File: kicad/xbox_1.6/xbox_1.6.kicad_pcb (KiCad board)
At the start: 2 copper layers, 18 parts, among them U2C1 intel_495_bga2, U4B1 ddr_100_tqfp, U4C1 nvidia_xgpu_nv2a, U5F1 ddr_100_tqfp, U6D1 ddr_100_tqfp, U6E1 nvidia_mcpx

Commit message: route more
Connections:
- U2C1 pad AA1: (no net) -> /CPU_AERR
- U2C1 pad AA2: (no net) -> /CPU_RS1
- U2C1 pad AA3: (no net) -> /CPU_DBSY
- U2C1 pad AA4: (no net) -> /VSS
- U2C1 pad AB1: (no net) -> /CPU_AP0
- U2C1 pad AB2: (no net) -> /CPU_ADS
- U2C1 pad AB3: (no net) -> /VSS
- U2C1 pad AB4: (no net) -> /VSS
- U2C1 pad AB5: (no net) -> /VSS
- U2C1 pad AC1: (no net) -> /VSS
- U2C1 pad AC2: (no net) -> /VSS
- U2C1 pad AC4: (no net) -> /VSS
- U2C1 pad AC5: (no net) -> /VSS
- U2C1 pad AD1: (no net) -> /VSS
- U2C1 pad AD2: (no net) -> /VSS
- U2C1 pad AD3: (no net) -> /VSS
- U2C1 pad AD4: (no net) -> /VSS
- U2C1 pad AD5: (no net) -> /VSS
- U2C1 pad H10: (no net) -> /CPU_VCC
- U2C1 pad H11: (no net) -> /VSS
- U2C1 pad H12: (no net) -> /CPU_VCC
- U2C1 pad H13: (no net) -> /VSS
- U2C1 pad H14: (no net) -> /CPU_VCC
- U2C1 pad H15: (no net) -> /VSS
- U2C1 pad H16: (no net) -> /CPU_VCC
- U2C1 pad H7: (no net) -> /VSS
- U2C1 pad H8: (no net) -> /CPU_VCC
- U2C1 pad H9: (no net) -> /VSS
- U2C1 pad J10: (no net) -> /VSS
- U2C1 pad J11: (no net) -> /CPU_VCC
- U2C1 pad J12: (no net) -> /VSS
- U2C1 pad J13: (no net) -> /CPU_VCC
- U2C1 pad J14: (no net) -> /VSS
- U2C1 pad J15: (no net) -> /CPU_VCC
- U2C1 pad J16: (no net) -> /VSS
- U2C1 pad J6: (no net) -> /CPU_VCCT
- U2C1 pad J7: (no net) -> /CPU_VCC
- U2C1 pad J8: (no net) -> /VSS
- U2C1 pad J9: (no net) -> /CPU_VCC
- U2C1 pad K10: (no net) -> /CPU_VCC
- U2C1 pad K11: (no net) -> /VSS
- U2C1 pad K12: (no net) -> /CPU_VCC
- U2C1 pad K13: (no net) -> /VSS
- U2C1 pad K14: (no net) -> /CPU_VCC
- U2C1 pad K15: (no net) -> /VSS
- U2C1 pad K16: (no net) -> /CPU_VCC
- U2C1 pad K7: (no net) -> /VSS
- U2C1 pad K8: (no net) -> /CPU_VCC
- U2C1 pad K9: (no net) -> /VSS
- U2C1 pad L10: (no net) -> /VSS
- U2C1 pad L11: (no net) -> /CPU_VCC
- U2C1 pad L12: (no net) -> /VSS
- U2C1 pad L13: (no net) -> /CPU_VCC
- U2C1 pad L14: (no net) -> /VSS
- U2C1 pad L15: (no net) -> /CPU_VCC
- U2C1 pad L16: (no net) -> /VSS
- U2C1 pad L7: (no net) -> /CPU_VCC
- U2C1 pad L8: (no net) -> /VSS
- U2C1 pad L9: (no net) -> /CPU_VCC
- U2C1 pad M10: (no net) -> /CPU_VCC
- U2C1 pad M11: (no net) -> /VSS
- U2C1 pad M12: (no net) -> /CPU_VCC
- U2C1 pad M13: (no net) -> /VSS
- U2C1 pad M14: (no net) -> /CPU_VCC
- U2C1 pad M15: (no net) -> /VSS
- U2C1 pad M16: (no net) -> /CPU_VCC
- U2C1 pad M7: (no net) -> /VSS
- U2C1 pad M8: (no net) -> /CPU_VCC
- U2C1 pad M9: (no net) -> /VSS
- U2C1 pad N10: (no net) -> /VSS
- U2C1 pad N11: (no net) -> /CPU_VCC
- U2C1 pad N12: (no net) -> /VSS
- U2C1 pad N13: (no net) -> /CPU_VCC
- U2C1 pad N14: (no net) -> /VSS
- U2C1 pad N15: (no net) -> /CPU_VCC
- U2C1 pad N16: (no net) -> /VSS
- U2C1 pad N7: (no net) -> /CPU_VCC
- U2C1 pad N8: (no net) -> /VSS
- U2C1 pad N9: (no net) -> /CPU_VCC
- U2C1 pad P10: (no net) -> /CPU_VCC
- U2C1 pad P11: (no net) -> /VSS
- U2C1 pad P12: (no net) -> /CPU_VCC
- U2C1 pad P13: (no net) -> /VSS
- U2C1 pad P14: (no net) -> /CPU_VCC
- U2C1 pad P15: (no net) -> /VSS
- U2C1 pad P16: (no net) -> /CPU_VCC
- U2C1 pad P7: (no net) -> /VSS
- U2C1 pad P8: (no net) -> /CPU_VCC
- U2C1 pad P9: (no net) -> /VSS
- U2C1 pad R10: (no net) -> /VSS
- U2C1 pad R11: (no net) -> /CPU_VCC
- U2C1 pad R12: (no net) -> /VSS
- U2C1 pad R13: (no net) -> /CPU_VCC
- U2C1 pad R14: (no net) -> /VSS
- U2C1 pad R15: (no net) -> /CPU_VCC
- U2C1 pad R16: (no net) -> /VSS
- U2C1 pad R7: (no net) -> /CPU_VCC
- U2C1 pad R8: (no net) -> /VSS
- U2C1 pad R9: (no net) -> /CPU_VCC
- U2C1 pad T10: (no net) -> /CPU_VCC
- U2C1 pad T11: (no net) -> /VSS
- U2C1 pad T12: (no net) -> /CPU_VCC
- U2C1 pad T13: (no net) -> /VSS
- U2C1 pad T14: (no net) -> /CPU_VCC
- U2C1 pad T15: (no net) -> /VSS
- U2C1 pad T16: (no net) -> /CPU_VCC
- U2C1 pad T7: (no net) -> /VSS
- U2C1 pad T8: (no net) -> /CPU_VCC
- U2C1 pad T9: (no net) -> /VSS
- U2C1 pad U10: (no net) -> /VSS
- U2C1 pad U11: (no net) -> /CPU_VCC
- U2C1 pad U12: (no net) -> /VSS
- U2C1 pad U13: (no net) -> /CPU_VCC
- U2C1 pad U14: (no net) -> /VSS
- U2C1 pad U15: (no net) -> /CPU_VCC
- U2C1 pad U16: (no net) -> /VSS
- U2C1 pad U7: (no net) -> /CPU_VCC
- U2C1 pad U8: (no net) -> /VSS
- U2C1 pad U9: (no net) -> /CPU_VCC
- U2C1 pad V1: (no net) -> /CPU_HIT
- U2C1 pad V2: (no net) -> /CPU_REQ2
- U2C1 pad V4: (no net) -> /CPU_REQ1
- U2C1 pad V5: (no net) -> /CPU_PWRGOOD
- U2C1 pad W1: (no net) -> /CPU_RS2
- U2C1 pad W2: (no net) -> /CPU_RP
- U2C1 pad W3: (no net) -> /CPU_REQ3
- U2C1 pad W4: (no net) -> /VSS
- U2C1 pad W5: (no net) -> /CPU_REQ4
- U2C1 pad Y1: (no net) -> /CPU_RSP
- U2C1 pad Y2: (no net) -> /CPU_AP1
- U2C1 pad Y3: (no net) -> /VSS
- U2C1 pad Y4: (no net) -> /CPU_HITM
- U2C1 pad Y5: (no net) -> /CPU_TESTLO1
- U4C1 pad A25: (no net) -> /CPU_HIT
- U4C1 pad A26: (no net) -> /CPU_REQ3
- U4C1 pad A27: (no net) -> /CPU_REQ4
- U4C1 pad A28: (no net) -> /CPU_DBSY
- U4C1 pad B24: (no net) -> /CPU_REQ2
- U4C1 pad B26: (no net) -> /CPU_RS2
- U4C1 pad B27: (no net) -> /CPU_ADS
- U4C1 pad B28: (no net) -> /CPU_RS1
- U4C1 pad C25: (no net) -> /CPU_REQ1
- U4C1 pad C27: (no net) -> /CPU_HITM
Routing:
- net /VSS: track 79.5 -> 166.6 mm, vias 47 -> 83
- net /CPU_REQ3: track 0.00 -> 80.7 mm, vias 0 -> 1
- net /CPU_HITM: track 0.00 -> 80.1 mm, vias 0 -> 1
- net /CPU_RS1: track 0.00 -> 80.1 mm, vias 0 -> 1
- net /CPU_ADS: track 0.00 -> 79.3 mm, vias 0 -> 1
- net /CPU_DBSY: track 0.00 -> 79.2 mm, vias 0 -> 1
- net /CPU_REQ4: track 0.00 -> 77.7 mm, vias 0 -> 1
- net /CPU_RS2: track 0.00 -> 77.4 mm, vias 0 -> 1
- net /CPU_REQ1: track 0.00 -> 77.0 mm, vias 0 -> 1
- net /CPU_VCC: track 0.00 -> 76.9 mm, vias 0 -> 16
- net /CPU_REQ2: track 0.00 -> 75.8 mm, vias 0 -> 1
- net /CPU_HIT: track 0.00 -> 75.7 mm, vias 0 -> 1
- net /CPU_AP1: track 0.00 -> 3.79 mm, vias 0 -> 1
- net /CPU_AP0: track 0.00 -> 0.85 mm, vias 0 -> 1
- net /CPU_TESTLO1: track 0.00 -> 0.84 mm, vias 0 -> 1
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
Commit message: route more
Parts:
- added C1C1: 0603_smd, xbox_footprint:0603_smd, F.Cu at (299.4, 122.5)
- added C1D1: 0603_smd, xbox_footprint:0603_smd, F.Cu at (302.0, 124.5)
- added C1D2: 0603_smd, xbox_footprint:0603_smd, F.Cu at (301.0, 130.8)
- added C1D3: 0603_smd, xbox_footprint:0603_smd, F.Cu at (295.8, 124.3)
- added R1C1: 0603_smd, xbox_footprint:0603_smd, F.Cu at (302.1, 120.7)
- added R1C10: 0603_smd, xbox_footprint:0603_smd, F.Cu at (295.9, 111.0)
- added R1C11: 0603_smd, xbox_footprint:0603_smd, F.Cu at (295.9, 113.0)
- added R1C12: 0603_smd, xbox_footprint:0603_smd, F.Cu at (295.9, 116.8)
- added R1C13: 0603_smd, xbox_footprint:0603_smd, F.Cu at (295.9, 114.8)
- added R1C14: 0603_smd, xbox_footprint:0603_smd, F.Cu at (295.8, 102.7)
- added R1C15: 0603_smd, xbox_footprint:0603_smd, F.Cu at (295.9, 101.0)
- added R1C16: 0603_smd, xbox_footprint:0603_smd, F.Cu at (295.8, 104.5)
- added R1C17: 0603_smd, xbox_footprint:0603_smd, F.Cu at (295.8, 106.3)
- added R1C2: 0603_smd, xbox_footprint:0603_smd, F.Cu at (299.5, 109.4)
- added R1C3: 0603_smd, xbox_footprint:0603_smd, F.Cu at (299.5, 111.0)
- added R1C4: 0603_smd, xbox_footprint:0603_smd, F.Cu at (299.5, 113.0)
- added R1C5: 0603_smd, xbox_footprint:0603_smd, F.Cu at (299.5, 114.8)
- added R1C6: 0603_smd, xbox_footprint:0603_smd, F.Cu at (299.5, 116.8)
- added R1C7: 0603_smd, xbox_footprint:0603_smd, F.Cu at (299.4, 118.9)
- added R1C8: 0603_smd, xbox_footprint:0603_smd, F.Cu at (299.4, 120.7)
- added R1C9: 0603_smd, xbox_footprint:0603_smd, F.Cu at (295.9, 109.2)
- added R1D1: 0603_smd, xbox_footprint:0603_smd, F.Cu at (301.1, 134.2)
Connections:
- U2C1 pad AA10: (no net) -> /CPU_INIT
- U2C1 pad AA12: (no net) -> /CPU_BSEL0
- U2C1 pad AA13: (no net) -> /VSS
- U2C1 pad AA15: (no net) -> /CPU_THERMDA
- U2C1 pad AA16: (no net) -> /CPU_EDGECTRLP
- U2C1 pad AA17: (no net) -> /CPU_BALL_AA17
- U2C1 pad AA18: (no net) -> /CPU_PICCLK
- U2C1 pad AA20: (no net) -> /VSS
- U2C1 pad AA6: (no net) -> /CPU_VCCT
- U2C1 pad AA7: (no net) -> /CPU_VCCT
- U2C1 pad AA8: (no net) -> /CPU_VCCT
- U2C1 pad AA9: (no net) -> /CPU_VREF
- U2C1 pad AB21: (no net) -> /CPU_PICD0
- U2C1 pad AD18: (no net) -> /CPU_VREF
- U2C1 pad W18: (no net) -> /VSS
- U2C1 pad W19: (no net) -> /CPU_BPM1
- U2C1 pad W20: (no net) -> /CPU_PRDY
- U2C1 pad W21: (no net) -> /CPU_BPM0
- U2C1 pad Y10: (no net) -> /VSS
- U2C1 pad Y11: (no net) -> /VSS
- U2C1 pad Y12: (no net) -> /VSS
- U2C1 pad Y13: (no net) -> /VSS
- U2C1 pad Y14: (no net) -> /VSS
- U2C1 pad Y15: (no net) -> /VSS
- U2C1 pad Y16: (no net) -> /VSS
- U2C1 pad Y17: (no net) -> /CPU_VREF
- U2C1 pad Y18: (no net) -> /CPU_VREF
- U2C1 pad Y19: (no net) -> /VSS
- U2C1 pad Y20: (no net) -> /CPU_PICD1
- U2C1 pad Y21: (no net) -> /CPU_BP3
- U2C1 pad Y9: (no net) -> /VSS
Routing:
- net /CPU_VREF: track 30.9 -> 50.7 mm, vias 6 -> 7
- net /CPU_INIT: track 0.00 -> 18.2 mm, vias 0 -> 1
- net /CPU_PICCLK: track 0.00 -> 16.0 mm, vias 0 -> 1
- net /CPU_PICD0: track 0.00 -> 13.5 mm, vias 0 -> 1
- net /VSS: track 166.6 -> 178.4 mm, vias 83 -> 89
- net /CPU_BSEL0: track 0.00 -> 0.92 mm, vias 0 -> 1
- net /CPU_BALL_AA17: track 0.00 -> 0.89 mm, vias 0 -> 1
- net /CPU_BPM0: track 0.00 -> 0.88 mm, vias 0 -> 1
- net /CPU_PICD1: track 0.00 -> 0.88 mm, vias 0 -> 1
- net /CPU_EDGECTRLP: track 0.00 -> 0.88 mm, vias 0 -> 1
- net /CPU_THERMDA: track 0.00 -> 0.87 mm, vias 0 -> 1
- net /CPU_BPM1: track 0.00 -> 0.84 mm, vias 0 -> 1

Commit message: front CPU area mostly finish
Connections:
- C1C1 pad 2: (no net) -> /CPU_VCCT
- C1D3 pad 2: (no net) -> /CPU_VCCT
- R1C11 pad 2: (no net) -> /CPU_IGNNE
- R1C13 pad 1: (no net) -> /CPU_SLP
- R1C16 pad 1: (no net) -> /CPU_NMI_LINT1
- R1C17 pad 1: (no net) -> /CPU_RTTIMPEDP
- R1C2 pad 1: (no net) -> /CPU_INTR_LINT0
- R1C3 pad 1: (no net) -> /CPU_TESTHI
- R1C5 pad 1: (no net) -> /CPU_FERR
- R1C7 pad 2: (no net) -> /CPU_VCCT
- R1C8 pad 1: (no net) -> /CPU_FLUSH
- R1C8 pad 2: (no net) -> /CPU_VCCT
- U2C1 pad AB10: (no net) -> /CPU_SMI
- U2C1 pad AB11: (no net) -> /VSS
- U2C1 pad AB12: (no net) -> /CPU_SLP
- U2C1 pad AB13: (no net) -> /VSS
- U2C1 pad AB14: (no net) -> /VSS
- U2C1 pad AB15: (no net) -> /CPU_BSEL1
- U2C1 pad AB16: (no net) -> /CPU_THERMDC
- U2C1 pad AB17: (no net) -> /VSS
- U2C1 pad AB18: (no net) -> /CPU_INTR_LINT0
- U2C1 pad AB19: (no net) -> /CPU_BALL_AB19
- U2C1 pad AB6: (no net) -> /CPU_VCCT
- U2C1 pad AB7: (no net) -> /CPU_VCCT
- U2C1 pad AB8: (no net) -> /CPU_VCCT
- U2C1 pad AB9: (no net) -> /VSS
- U2C1 pad AC10: (no net) -> /VSS
- U2C1 pad AC11: (no net) -> /CPU_STPCLK
- U2C1 pad AC12: (no net) -> /CPU_FERR
- U2C1 pad AC13: (no net) -> /CPU_IGNNE
- U2C1 pad AC14: (no net) -> /VSS
- U2C1 pad AC16: (no net) -> /VSS
- U2C1 pad AC18: (no net) -> /VSS
- U2C1 pad AC19: (no net) -> /CPU_NMI_LINT1
- U2C1 pad AC21: (no net) -> /VSS
- U2C1 pad AC6: (no net) -> /CPU_VCCT
- U2C1 pad AC7: (no net) -> /CPU_VCCT
- U2C1 pad AC8: (no net) -> /CPU_VCCT
- U2C1 pad AC9: (no net) -> /CPU_FLUSH
- U2C1 pad AD10: (no net) -> /CPU_A20M
- U2C1 pad AD16: (no net) -> /VSS
- U2C1 pad AD17: (no net) -> /CPU_TESTHI
- U2C1 pad AD19: (no net) -> /CPU_RTTIMPEDP
- U2C1 pad AD20: (no net) -> /CPU_BALL_AD20
- U2C1 pad AD21: (no net) -> /VSS
- U2C1 pad AD6: (no net) -> /CPU_VCCT
- U2C1 pad AD7: (no net) -> /CPU_VCCT
- U2C1 pad AD8: (no net) -> /CPU_VCCT
- U2C1 pad AD9: (no net) -> /CPU_IERR
- U2C1 pad G10: (no net) -> /CPU_VCCT
- U2C1 pad G11: (no net) -> /CPU_VCCT
- U2C1 pad G12: (no net) -> /CPU_VCCT
- U2C1 pad G13: (no net) -> /CPU_VCCT
- U2C1 pad G14: (no net) -> /CPU_VCCT
- U2C1 pad G15: (no net) -> /CPU_VCCT
- U2C1 pad G16: (no net) -> /CPU_VCCT
- U2C1 pad G17: (no net) -> /CPU_VCCT
- U2C1 pad G6: (no net) -> /CPU_VCCT
- U2C1 pad G7: (no net) -> /CPU_VCCT
- U2C1 pad G8: (no net) -> /CPU_VCCT
- U2C1 pad G9: (no net) -> /CPU_VCCT
- U2C1 pad H17: (no net) -> /CPU_VCCT
- U2C1 pad H6: (no net) -> /CPU_VCCT
- U2C1 pad J17: (no net) -> /CPU_VCCT
- U2C1 pad K17: (no net) -> /CPU_VCCT
- U2C1 pad K6: (no net) -> /CPU_VCCT
- U2C1 pad L17: (no net) -> /CPU_VCCT
- U2C1 pad L6: (no net) -> /CPU_VCCT
- U2C1 pad M17: (no net) -> /CPU_VCCT
- U2C1 pad M6: (no net) -> /CPU_VCCT
- U2C1 pad N17: (no net) -> /CPU_VCCT
- U2C1 pad P6: (no net) -> /CPU_VCCT
- U2C1 pad R6: (no net) -> /CPU_VCCT
- U2C1 pad T6: (no net) -> /CPU_VCCT
- U2C1 pad U17: (no net) -> /CPU_VCCT
- U2C1 pad U6: (no net) -> /CPU_VCCT
- U2C1 pad W10: (no net) -> /CPU_VCCT
- U2C1 pad W11: (no net) -> /CPU_VCCT
- U2C1 pad W12: (no net) -> /CPU_VCCT
- U2C1 pad W13: (no net) -> /CPU_VCCT
- U2C1 pad W14: (no net) -> /CPU_VCCT
- U2C1 pad W15: (no net) -> /CPU_VCCT
- U2C1 pad W16: (no net) -> /CPU_VCCT
- U2C1 pad W17: (no net) -> /CPU_VCCT
- U2C1 pad W6: (no net) -> /CPU_VCCT
- U2C1 pad W7: (no net) -> /CPU_VCCT
- U2C1 pad W8: (no net) -> /CPU_VCCT
- U2C1 pad W9: (no net) -> /CPU_VCCT
- U2C1 pad Y6: (no net) -> /CPU_VCCT
- U2C1 pad Y7: (no net) -> /CPU_VCCT
- U2C1 pad Y8: (no net) -> /CPU_VCCT
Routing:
- net /CPU_INTR_LINT0: track 0.00 -> 16.7 mm, vias 0 -> 1
- net /CPU_FERR: track 0.00 -> 16.1 mm, vias 0 -> 1
- net /CPU_IGNNE: track 0.00 -> 15.4 mm, vias 0 -> 1
- net /CPU_FLUSH: track 0.00 -> 12.5 mm, vias 0 -> 1
- net /VSS: track 178.4 -> 189.3 mm, vias 89 -> 99
- net /CPU_TESTHI: track 0.00 -> 9.92 mm, vias 0 -> 1
- net /CPU_SLP: track 0.00 -> 8.79 mm, vias 0 -> 1
- net /CPU_NMI_LINT1: track 0.00 -> 7.46 mm
- net /CPU_RTTIMPEDP: track 0.00 -> 6.50 mm, vias 0 -> 1
- net /CPU_IERR: track 0.00 -> 4.86 mm, vias 0 -> 1
- net /CPU_BALL_AD20: track 0.00 -> 1.83 mm, vias 0 -> 1
- net /CPU_BALL_AB19: track 0.00 -> 0.96 mm, vias 0 -> 1
- net /CPU_THERMDC: track 0.00 -> 0.89 mm, vias 0 -> 1
- net /CPU_SMI: track 0.00 -> 0.87 mm, vias 0 -> 1
- net /CPU_BSEL1: track 0.00 -> 0.87 mm, vias 0 -> 1
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- added copper zone on F.Cu, net /CPU_VCCT

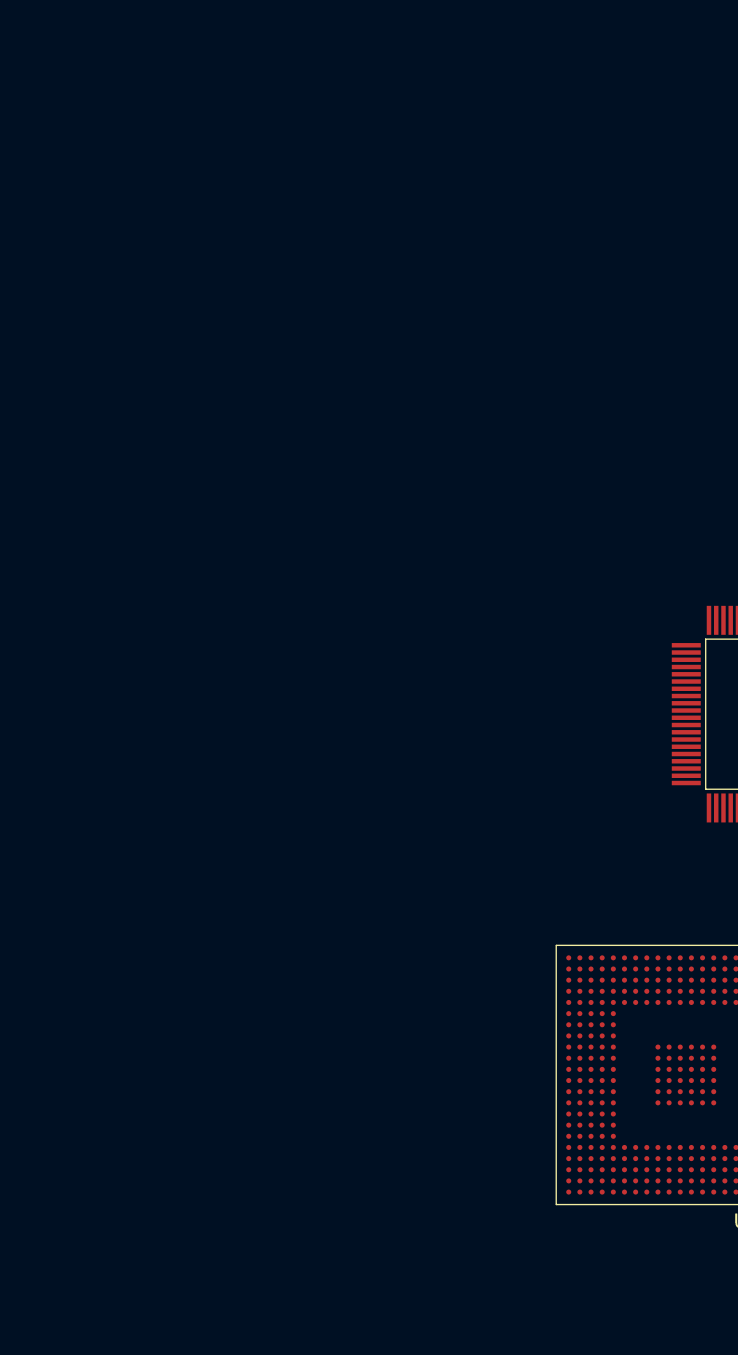
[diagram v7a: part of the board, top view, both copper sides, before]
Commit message: start to route IDE port
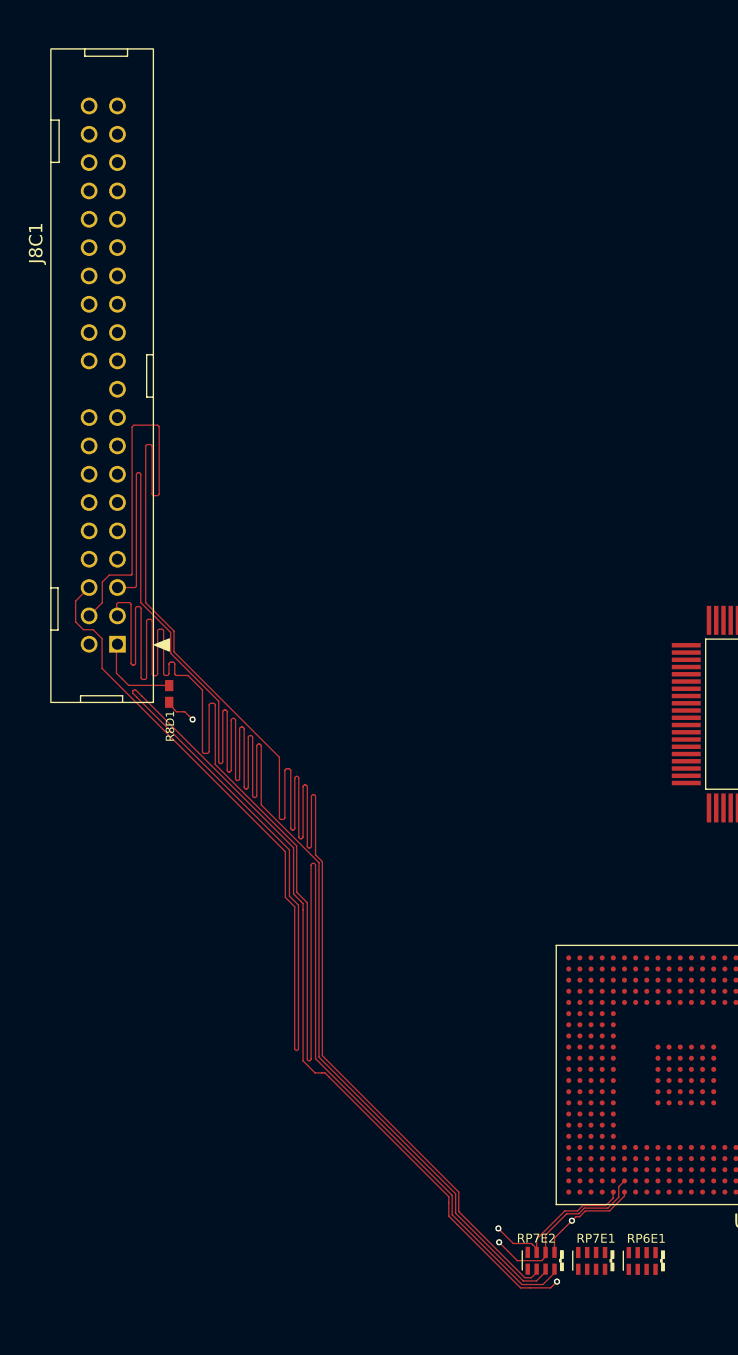
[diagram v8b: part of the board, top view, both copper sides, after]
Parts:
- added J8C1: IDC_40_Pin, xbox_footprint:IDC_40_Pin, F.Cu at (99.7, 121.6)
- added R8D1: 0603_smd, xbox_footprint:0603_smd, F.Cu at (104.4, 126.1)
- added RP6E1: 0603_4_array, xbox_footprint:0603_4_array, F.Cu at (148.0, 177.7)
- added RP7E1: 0603_4_array, xbox_footprint:0603_4_array, F.Cu at (143.4, 177.7)
- added RP7E2: 0603_4_array, xbox_footprint:0603_4_array, F.Cu at (138.9, 177.6)
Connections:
- U6E1 pad A17: (no net) -> /IDE_D7_R
- U6E1 pad A18: (no net) -> /IDE_D8_R
- U6E1 pad B17: (no net) -> /IDE_D6_R
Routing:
- net /IDE_D8: track 0.00 -> 162.8 mm
- net /IDE_D9: track 0.00 -> 161.4 mm, vias 0 -> 1
- net /IDE_D7: track 0.00 -> 160.2 mm
- net /IDE_D6: track 0.00 -> 150.0 mm
- net /IDE_D6_R: track 0.00 -> 16.6 mm, vias 0 -> 1
- net /IDE_D8_R: track 0.00 -> 14.7 mm, vias 0 -> 1
- net /IDE_D7_R: track 0.00 -> 9.47 mm, vias 0 -> 1
- net /IDE_RESET: track 0.00 -> 7.79 mm
- net /IDE_RESET_R: track 0.00 -> 2.85 mm, vias 0 -> 1
